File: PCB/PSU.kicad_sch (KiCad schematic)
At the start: 41 parts, among them J1 USB In, Q1 AO3400A, Q2 AO3400A, Q3 AO3400A, U1 TPD4E05U06DQAR, U12 TPS61040DBV, U6 AP2127K-ADJ, U7 AMS1117-3.3, U8 TUSB320LA, U9 TPS259533

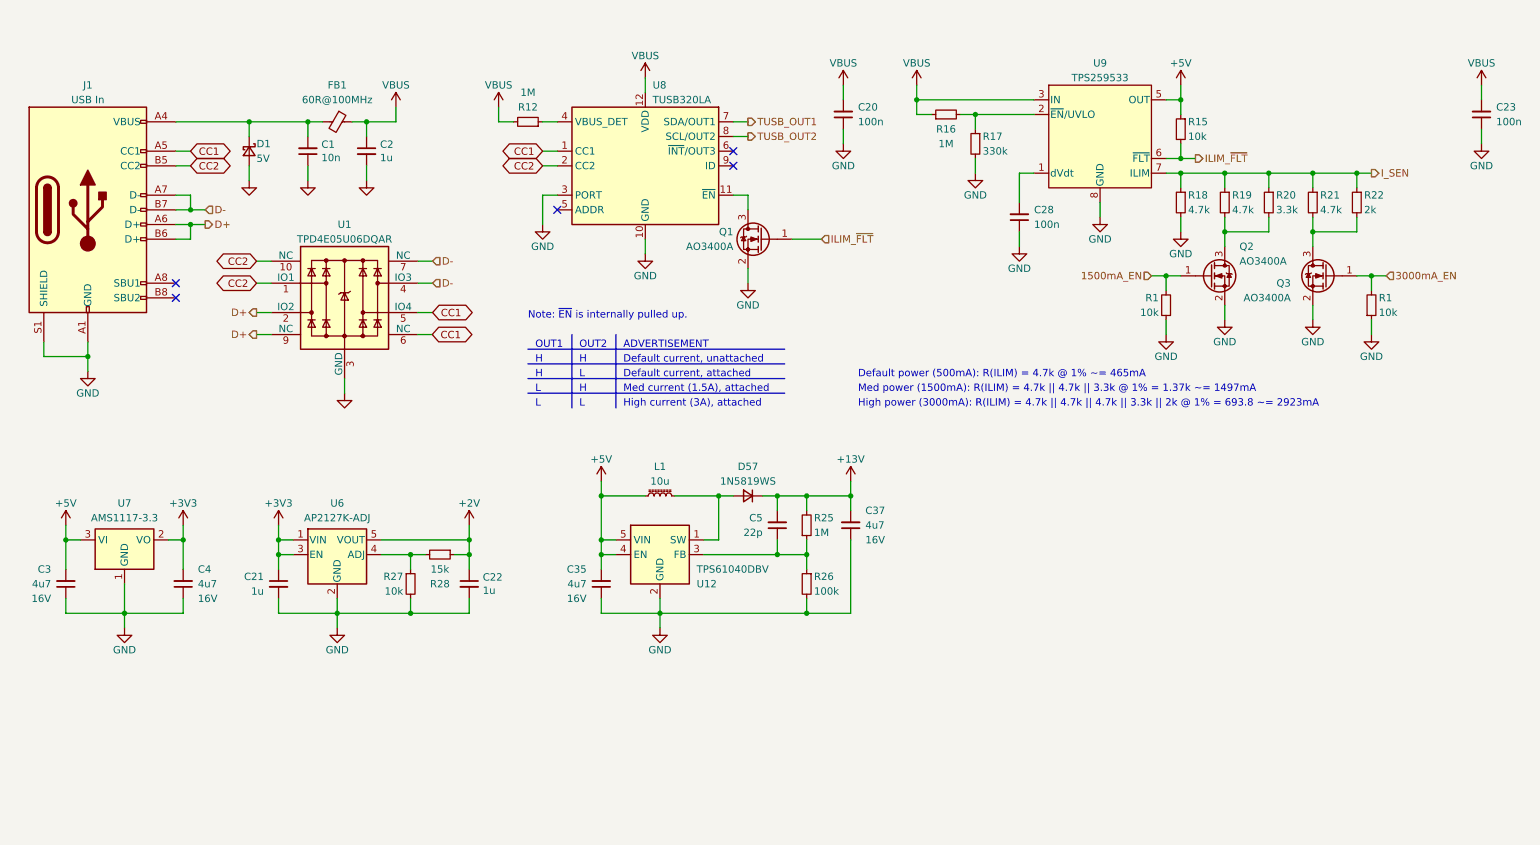
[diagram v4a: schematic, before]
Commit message: 3/4-done update.
Added current and voltage measurement for VBUS in and current measurement for the RGB output. Added PMOS power switch to fully turn off RGB LEDs when not in use. Rerouted the PCB. Moved OLED ribbon cable cutout and expanded it length-wise. Changed position of various components for better routing. Changed bulk capacitance of RGB LEDs to 5 x 22u capacitors. Changed the four N mosfets to two much smaller dual N mosfets. Still need to do RGB routing!
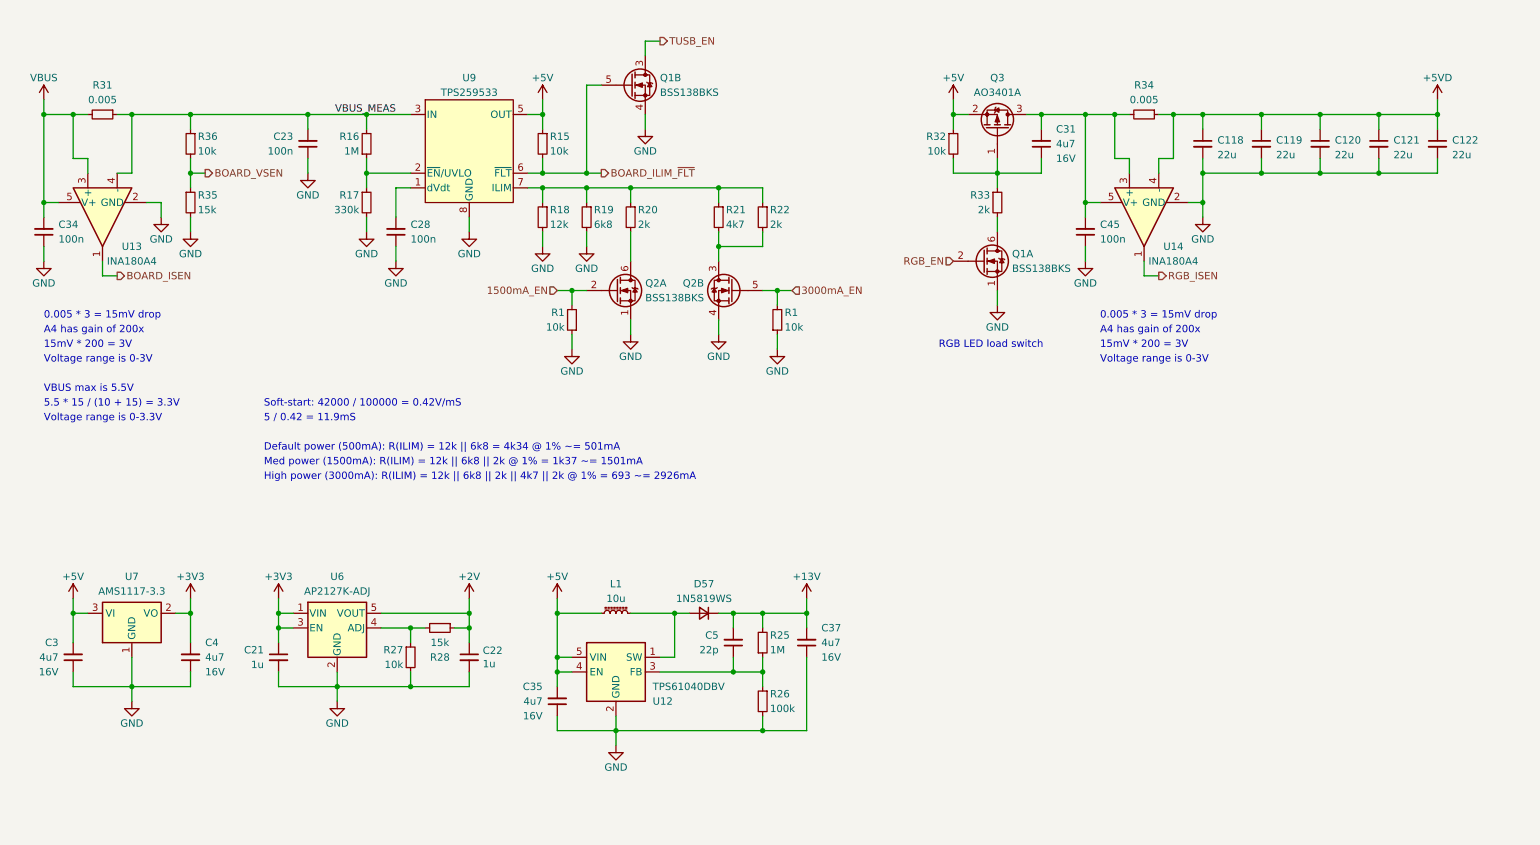
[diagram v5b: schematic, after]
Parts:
- removed C1: 10n, Capacitor_SMD:C_0402_1005Metric, symbol Device:C_Small
- removed C2: 1u, Capacitor_SMD:C_0603_1608Metric, symbol Device:C_Small
- removed C20: 100n, Capacitor_SMD:C_0402_1005Metric, symbol Device:C_Small
- removed D1: 5V, Diode_SMD:D_SOD-523, symbol Device:D_Schottky_Small
- removed FB1: 60R@100MHz, Inductor_SMD:L_0805_2012Metric, symbol Device:FerriteBead_Small
- removed J1: USB In, Honeydew:HRO-TYPE-C-31-M-13x, symbol Connector:USB_C_Receptacle_USB2.0
- removed Q1, Q2, Q3: AO3400A, Package_TO_SOT_SMD:SOT-23, symbol Transistor_FET:AO3400A
- removed R12: 1M, Resistor_SMD:R_0402_1005Metric, symbol Device:R_Small
- removed U1: TPD4E05U06DQAR, Honeydew:USON-10_2.5x1.0mm_P0.5mm, symbol Casaba:TPD4E05U06DQAR
- removed U8: TUSB320LA, Honeydew:Texas_X2QFN-12_1.6x1.6mm_P0.4mm, symbol Interface_USB:TUSB320I
- added C118, C119, C120, C121, C122: 22u, Capacitor_SMD:C_0805_2012Metric, symbol Device:C_Small
- added C31: 4u7, Capacitor_SMD:C_0603_1608Metric, symbol Device:C_Small
- added C34, C45: 100n, Capacitor_SMD:C_0402_1005Metric, symbol Device:C_Small
- added Q1, Q2: BSS138BKS, Package_TO_SOT_SMD:SOT-363_SC-70-6, symbol Device:Q_Dual_NMOS_S1G1D2S2G2D1
- added Q3: AO3401A, Package_TO_SOT_SMD:SOT-23, symbol Transistor_FET:AO3401A
- added R31, R34: 0.005, Resistor_SMD:R_0805_2012Metric, symbol Device:R_Small
- added R32, R36: 10k, Resistor_SMD:R_0402_1005Metric, symbol Device:R_Small
- added R33: 2k, Resistor_SMD:R_0402_1005Metric, symbol Device:R_Small
- added R35: 15k, Resistor_SMD:R_0402_1005Metric, symbol Device:R_Small
- added U13, U14: INA180A4, Package_TO_SOT_SMD:SOT-23-5, symbol Amplifier_Current:INA180A4
- R18: value 4.7k -> 12k; LCSC C25900 -> C25752
- R19: value 4.7k -> 6k8; LCSC C25900 -> C25917
- R20: value 3.3k -> 2k; LCSC C25890 -> C4109
- R21: value 4.7k -> 4k7
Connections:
- net +5V: now also Q3.2 (S), R32.1
- net 1500mA_EN: now also Q2.2 (G)
- net 3000mA_EN: now also Q2.5 (G)
- net GND: now also R19.2, C118.2, C119.2, C120.2, C121.2, C122.2, C34.1, C45.1, Q1.1 (S), Q1.4 (S), Q2.1 (S), Q2.4 (S), R35.2, U13.2 (GND), U14.2 (GND)
- net at R20.2: now also Q2.6 (D); no longer R19.2
- net at R21.2, R22.2: now also Q2.3 (D)
- net at R17.1, U9.2 (~{EN}/UVLO): now also R16.1; no longer R16.2
- net ILIM_~{FLT} renamed BOARD_ILIM_~{FLT}
- net BOARD_ILIM_~{FLT}: now also Q1.5 (G)
- net IN renamed VBUS_MEAS
- net VBUS_MEAS: now also R16.2, R31.1, R36.1, U13.4 (-); no longer R16.1
- net I_SEN: no longer names the net of R18.1, R19.1, R20.1, R21.1, R22.1, U9.7 (ILIM)
- new net: C31.2, C45.2, Q3.3 (D), R34.2, U14.3 (+), U14.5 (V+)
- new net: C31.1, Q3.1 (G), R32.2, R33.1
- new net: Q1.6 (D), R33.2
- new net +5VD: C118.1, C119.1, C120.1, C121.1, C122.1, R34.1, U14.4 (-)
- new net BOARD_ISEN: U13.1
- new net BOARD_VSEN: R35.1, R36.2
- new net RGB_EN: Q1.2 (G)
- new net RGB_ISEN: U14.1
- new net TUSB_EN: Q1.3 (D)
- new net VBUS: C34.2, R31.2, U13.3 (+), U13.5 (V+)
- no-connect marks 5 -> 0
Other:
- note added: "0.005 * 3 = 15mV drop"
- note added: "15mV * 200 = 3V"
- note added: "5 / 0.42 = 11.9mS"
- note added: "5.5 * 15 / (10 + 15) = 3.3V"
- note added: "A4 has gain of 200x"
- note added: "Default power (500mA): R(ILIM) = 12k || 6k8 = 4k34 @ 1% ~= 501mA"
- note added: "High power (3000mA): R(ILIM) = 12k || 6k8 || 2k || 4k7 || 2k @ 1% = 693 ~= 2926mA"
- note added: "Med power (1500mA): R(ILIM) = 12k || 6k8 || 2k @ 1% = 1k37 ~= 1501mA"
- note added: "RGB LED load switch"
- note added: "Soft-start: 42000 / 100000 = 0.42V/mS"
- note added: "VBUS max is 5.5V"
- note added: "Voltage range is 0-3.3V"
- note added: "Voltage range is 0-3V"
- note removed: "ADVERTISEMENT"
- note removed: "Default current, attached"
- note removed: "Default current, unattached"
- note removed: "Default power (500mA): R(ILIM) = 4.7k @ 1% ~= 465mA"
- note removed: "H"
- note removed: "High current (3A), attached"
- note removed: "High power (3000mA): R(ILIM) = 4.7k || 4.7k || 4.7k || 3.3k || 2k @ 1% = 693.8 ~= 2923mA"
- note removed: "L"
- note removed: "Med current (1.5A), attached"
- note removed: "Med power (1500mA): R(ILIM) = 4.7k || 4.7k || 3.3k @ 1% = 1.37k ~= 1497mA"
- note removed: "Note: ~{EN} is internally pulled up."
- note removed: "OUT1"
- note removed: "OUT2"
- moved on the sheet: C21, C22, C28, C3, C35, C37, C4, C5, D57, L1, R1, R15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

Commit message: 05/05/2023 update.
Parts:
- removed Q1: BSS138BKS, Package_TO_SOT_SMD:SOT-363_SC-70-6, symbol Device:Q_Dual_NMOS_S1G1D2S2G2D1
- removed Q3: AO3401A, Package_TO_SOT_SMD:SOT-23, symbol Transistor_FET:AO3401A
- removed R33: 2k, Resistor_SMD:R_0402_1005Metric, symbol Device:R_Small
- removed U14: INA180A4, Package_TO_SOT_SMD:SOT-23-5, symbol Amplifier_Current:INA180A4
- added JP2: 13V EN, Honeydew:SolderJumper-2_P1.2mm_Open_Pad1.0x1.0mm, symbol Honeydew:SolderJumper_2_Open
- added R9: 1k, Resistor_SMD:R_0402_1005Metric, symbol Device:R_Small
- added U14: TPS259533, Honeydew:WSON-8-1EP_2x2mm_P0.5mm_EP0.9x1.6mm, symbol Honeydew:TPS259533
- C118: value 22u -> 100n; footprint Capacitor_SMD:C_0805_2012Metric -> Capacitor_SMD:C_0402_1005Metric; LCSC C45783 -> C307331; Voltage 25V -> 50V
- C119: value 22u -> 1u; footprint Capacitor_SMD:C_0805_2012Metric -> Capacitor_SMD:C_0603_1608Metric; LCSC C45783 -> C15849; Voltage 25V -> 50V
- C31: value 4u7 -> 1u; LCSC C19666 -> C15849; Voltage 16V -> 50V
- R32: value 10k -> 2k; LCSC C25744 -> C4109
- R34: value 0.005 -> 10k; footprint Resistor_SMD:R_0805_2012Metric -> Resistor_SMD:R_0402_1005Metric; LCSC C2939747 -> C25744
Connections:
- net +3V3: now also R15.1, R34.1
- net +5V: now also C31.1, C45.2, JP2.1 (A), U14.3 (IN), U14.4 (IN); no longer C35.2, L1.2, R15.1, R32.1, U12.4 (EN), U12.5 (VIN)
- net +5VD: now also U14.5 (OUT); no longer C118.1, R34.1
- net GND: now also C118.1, C31.2, R32.2, R9.1, U14.8 (GND), U14.9 (GND); no longer C118.2
- net RGB_EN: now also U14.2 (~{EN}/UVLO)
- net 1500mA_EN renamed 1.5A_EN
- net 3000mA_EN renamed 3A_EN
- new net: C35.2, JP2.2 (B), L1.2, U12.4 (EN), U12.5 (VIN)
- new net: C118.2, U14.1 (dVdt)
- new net: R32.1, R9.2, U14.7 (ILIM)
- new net RGB_ILIM_~{FLT}: R34.2, U14.6 (~{FLT})
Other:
- note added: "ADVERTISEMENT"
- note added: "Default current"
- note added: "H"
- note added: "High current (3A)"
- note added: "L"
- note added: "Med current (1.5A)"
- note added: "OUT1"
- note added: "OUT2"
- note added: "R(ILIM) = 1k || 2k @ 1% = 666.67 ~= 3039mA"
- note added: "X"
- note removed: "RGB LED load switch"
- moved on the sheet: C21, C22, C23, C28, C3, C34, C35, C37, C4, C5, D57, L1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

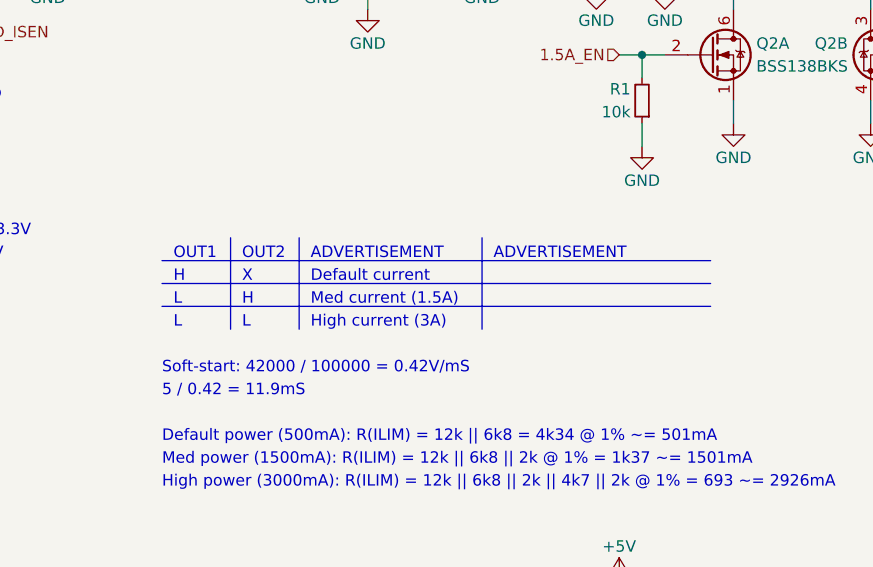
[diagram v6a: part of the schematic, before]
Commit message: Finished routing RGB LEDs.
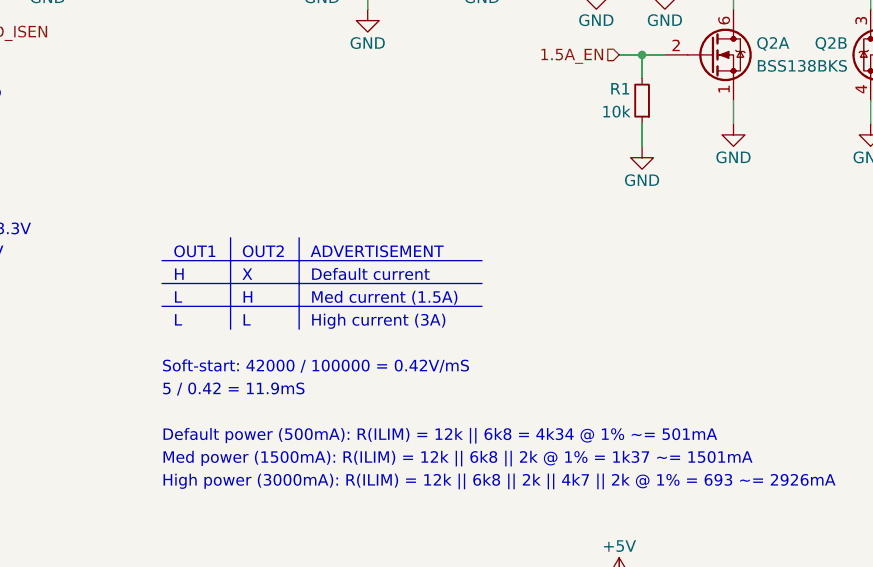
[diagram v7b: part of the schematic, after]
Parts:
- Q2: footprint Package_TO_SOT_SMD:SOT-363_SC-70-6 -> Honeydew:SOT-363_SC-70-6
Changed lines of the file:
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@@
     (stroke (width 0) (type default))
   )
-  (polyline (pts (xy 55.88 81.28) (xy 116.84 81.28))
+  (polyline (pts (xy 55.88 81.28) (xy 91.44 81.28))
     (stroke (width 0) (type default))
   )
@@
     (stroke (width 0) (type default))
   )
-  (polyline (pts (xy 91.44 78.74) (xy 91.44 88.9))
-    (stroke (width 0) (type default))
-  )
   (wire (pts (xy 22.86 35.56) (xy 25.4 35.56))
     (stroke (width 0) (type default))
@@
     (stroke (width 0) (type default))
   )
-  (polyline (pts (xy 55.88 83.82) (xy 116.84 83.82))
+  (polyline (pts (xy 55.88 83.82) (xy 91.44 83.82))
     (stroke (width 0) (type default))
   )
@@
     (stroke (width 0) (type default))
   )
-  (polyline (pts (xy 55.88 86.36) (xy 116.84 86.36))
+  (polyline (pts (xy 55.88 86.36) (xy 91.44 86.36))
     (stroke (width 0) (type default))
   )
@@
   )
   (text "ADVERTISEMENT" (at 72.39 81.28 0)
-    (effects (font (size 1.27 1.27)) (justify left bottom))
-  )
-  (text "ADVERTISEMENT" (at 92.71 81.28 0)
     (effects (font (size 1.27 1.27)) (justify left bottom))
   )
@@
       (effects (font (size 1.27 1.27)))
     )
-    (property "Footprint" "Package_TO_SOT_SMD:SOT-363_SC-70-6" (at 132.08 58.42 0)
+    (property "Footprint" "Honeydew:SOT-363_SC-70-6" (at 132.08 58.42 0)
       (effects (font (size 1.27 1.27)) hide)
     )
@@
       (effects (font (size 1.27 1.27)) (justify left) hide)
     )
-    (property "Footprint" "Package_TO_SOT_SMD:SOT-363_SC-70-6" (at 121.92 58.42 0)
-      (effects (font (size 1.27 1.27)) hide)
-    )
+    (property "Footprint" "Honeydew:SOT-363_SC-70-6" (at 121.92 58.42 0)
+      (effects (font (size 1.27 1.27)) hide)
+    )
